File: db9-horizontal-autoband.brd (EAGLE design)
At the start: 33 x 37 mm, 19 parts, among them U8 PCA9536

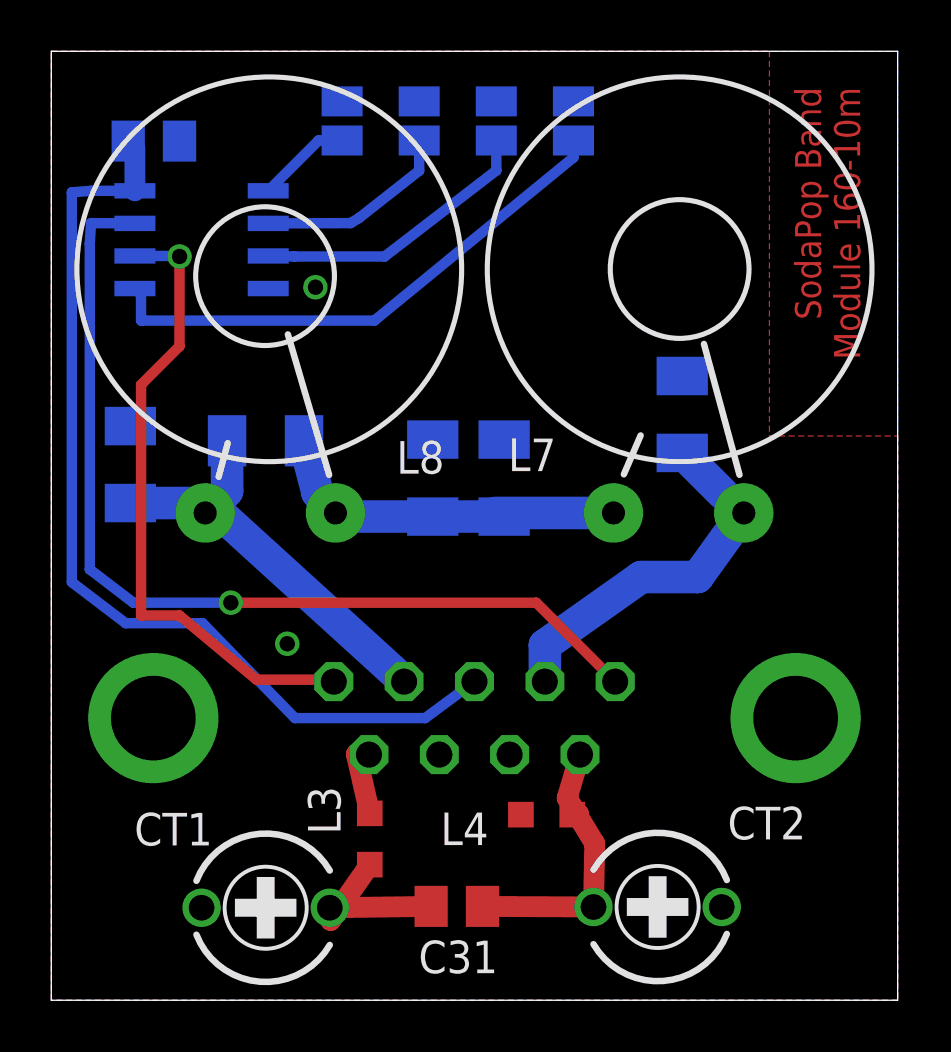
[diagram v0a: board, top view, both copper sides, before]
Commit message: Fixed hole size on trimmer cap
Fixed hole size on trimmer cap in library PCA9536.lbr and updated the
two autoband boards to use the corrected package. Package can be
replaced on other boards with the one in this library to fix the
problem. Also moved the text on the horizontal board to the bPlace
layer. Couldn't do this on the smaller board as no where to put it!
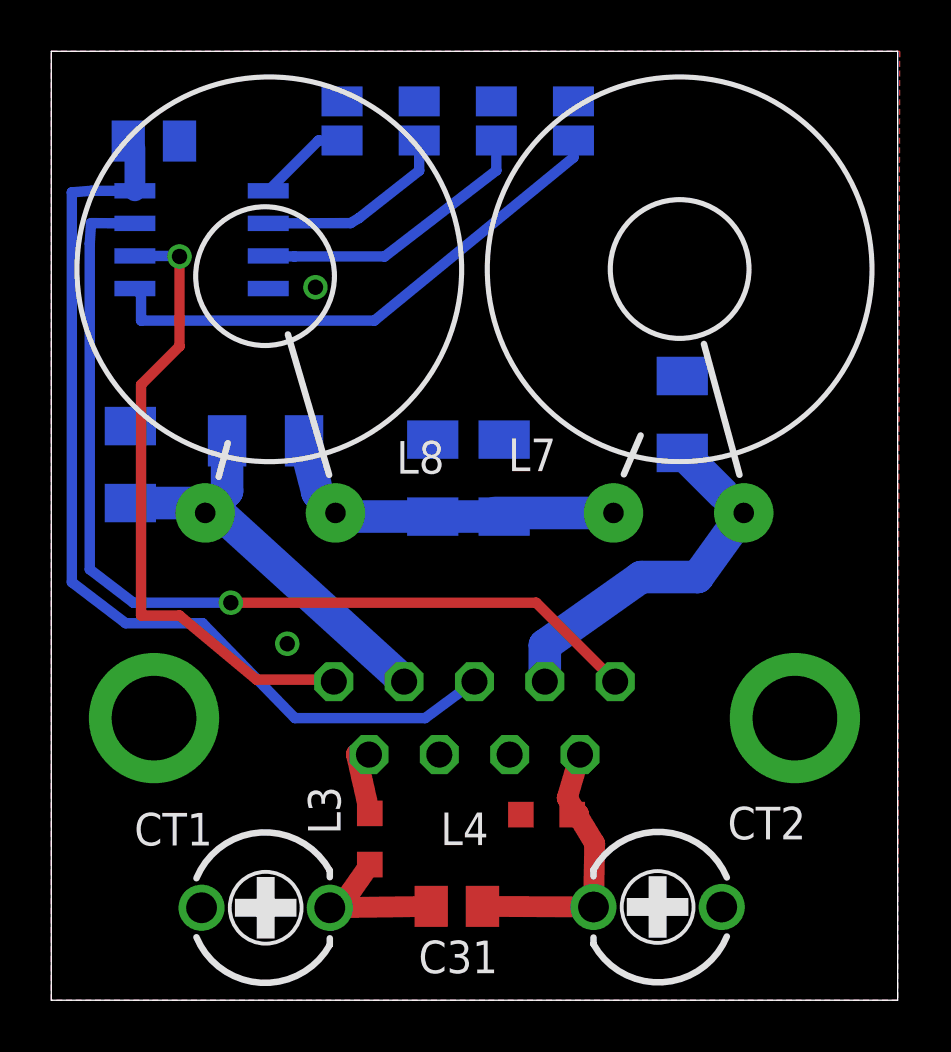
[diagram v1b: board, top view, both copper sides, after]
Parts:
- CT1, CT2: device rcl:CTRIMTZ03 -> PCA9536:CTRIMTZ03
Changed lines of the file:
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@@
 <setting verticaltext="up"/>
 </settings>
-<grid distance="0.5" unitdist="mm" unit="mm" style="lines" multiple="1" display="no" altdistance="0.1" altunitdist="mm" altunit="mm"/>
+<grid distance="1" unitdist="mm" unit="mm" style="lines" multiple="1" display="no" altdistance="0.1" altunitdist="mm" altunit="mm"/>
 <layers>
 <layer number="1" name="Top" color="4" fill="1" visible="yes" active="yes"/>
-<layer number="2" name="Route2" color="1" fill="3" visible="no" active="yes"/>
-<layer number="3" name="Route3" color="4" fill="3" visible="no" active="yes"/>
-<layer number="14" name="Route14" color="1" fill="6" visible="no" active="yes"/>
-<layer number="15" name="Route15" color="4" fill="6" visible="no" active="yes"/>
-<layer number="16" name="Bottom" color="1" fill="1" visible="no" active="yes"/>
+<layer number="2" name="Route2" color="1" fill="3" visible="yes" active="yes"/>
+<layer number="3" name="Route3" color="4" fill="3" visible="yes" active="yes"/>
+<layer number="14" name="Route14" color="1" fill="6" visible="yes" active="yes"/>
+<layer number="15" name="Route15" color="4" fill="6" visible="yes" active="yes"/>
+<layer number="16" name="Bottom" color="1" fill="1" visible="yes" active="yes"/>
 <layer number="17" name="Pads" color="2" fill="1" visible="yes" active="yes"/>
 <layer number="18" name="Vias" color="2" fill="1" visible="yes" active="yes"/>
@@
 <layer number="20" name="Dimension" color="15" fill="1" visible="yes" active="yes"/>
 <layer number="21" name="tPlace" color="7" fill="1" visible="yes" active="yes"/>
-<layer number="22" name="bPlace" color="7" fill="1" visible="no" active="yes"/>
+<layer number="22" name="bPlace" color="7" fill="1" visible="yes" active="yes"/>
 <layer number="23" name="tOrigins" color="15" fill="1" visible="yes" active="yes"/>
-<layer number="24" name="bOrigins" color="15" fill="1" visible="no" active="yes"/>
+<layer number="24" name="bOrigins" color="15" fill="1" visible="yes" active="yes"/>
 <layer number="25" name="tNames" color="7" fill="1" visible="yes" active="yes"/>
-<layer number="26" name="bNames" color="7" fill="1" visible="no" active="yes"/>
-<layer number="27" name="tValues" color="7" fill="1" visible="no" active="yes"/>
-<layer number="28" name="bValues" color="7" fill="1" visible="no" active="yes"/>
+<layer number="26" name="bNames" color="7" fill="1" visible="yes" active="yes"/>
+<layer number="27" name="tValues" color="7" fill="1" visible="yes" active="yes"/>
+<layer number="28" name="bValues" color="7" fill="1" visible="yes" active="yes"/>
 <layer number="29" name="tStop" color="7" fill="3" visible="yes" active="yes"/>
-<layer number="30" name="bStop" color="7" fill="6" visible="no" active="yes"/>
-<layer number="31" name="tCream" color="7" fill="4" visible="no" active="yes"/>
-<layer number="32" name="bCream" color="7" fill="5" visible="no" active="yes"/>
-<layer number="33" name="tFinish" color="6" fill="3" visible="no" active="yes"/>
-<layer number="34" name="bFinish" color="6" fill="6" visible="no" active="yes"/>
-<layer number="35" name="tGlue" color="7" fill="4" visible="no" active="yes"/>
-<layer number="36" name="bGlue" color="7" fill="5" visible="no" active="yes"/>
-<layer number="37" name="tTest" color="7" fill="1" visible="no" active="yes"/>
-<layer number="38" name="bTest" color="7" fill="1" visible="no" active="yes"/>
+<layer number="30" name="bStop" color="7" fill="6" visible="yes" active="yes"/>
+<layer number="31" name="tCream" color="7" fill="4" visible="yes" active="yes"/>
+<layer number="32" name="bCream" color="7" fill="5" visible="yes" active="yes"/>
+<layer number="33" name="tFinish" color="6" fill="3" visible="yes" active="yes"/>
+<layer number="34" name="bFinish" color="6" fill="6" visible="yes" active="yes"/>
+<layer number="35" name="tGlue" color="7" fill="4" visible="yes" active="yes"/>
+<layer number="36" name="bGlue" color="7" fill="5" visible="yes" active="yes"/>
+<layer number="37" name="tTest" color="7" fill="1" visible="yes" active="yes"/>
+<layer number="38" name="bTest" color="7" fill="1" visible="yes" active="yes"/>
 <layer number="39" name="tKeepout" color="4" fill="11" visible="yes" active="yes"/>
-<layer number="40" name="bKeepout" color="1" fill="11" visible="no" active="yes"/>
+<layer number="40" name="bKeepout" color="1" fill="11" visible="yes" active="yes"/>
 <layer number="41" name="tRestrict" color="4" fill="10" visible="yes" active="yes"/>
-<layer number="42" name="bRestrict" color="1" fill="10" visible="no" active="yes"/>
-<layer number="43" name="vRestrict" color="2" fill="10" visible="no" active="yes"/>
-<layer number="44" name="Drills" color="7" fill="1" visible="no" active="yes"/>
-<layer number="45" name="Holes" color="7" fill="1" visible="no" active="yes"/>
-<layer number="46" name="Milling" color="3" fill="1" visible="no" active="yes"/>
-<layer number="47" name="Measures" color="7" fill="1" visible="no" active="yes"/>
-<layer number="48" name="Document" color="7" fill="1" visible="no" active="yes"/>
-<layer number="49" name="Reference" color="7" fill="1" visible="no" active="yes"/>
-<layer number="51" name="tDocu" color="7" fill="1" visible="no" active="yes"/>
-<layer number="52" name="bDocu" color="7" fill="1" visible="no" active="yes"/>
+<layer number="42" name="bRestrict" color="1" fill="10" visible="yes" active="yes"/>
+<layer number="43" name="vRestrict" color="2" fill="10" visible="yes" active="yes"/>
+<layer number="44" name="Drills" color="7" fill="1" visible="yes" active="yes"/>
+<layer number="45" name="Holes" color="7" fill="1" visible="yes" active="yes"/>
+<layer number="46" name="Milling" color="3" fill="1" visible="yes" active="yes"/>
+<layer number="47" name="Measures" color="7" fill="1" visible="yes" active="yes"/>
+<layer number="48" name="Document" color="7" fill="1" visible="yes" active="yes"/>
+<layer number="49" name="Reference" color="7" fill="1" visible="yes" active="yes"/>
+<layer number="51" name="tDocu" color="7" fill="1" visible="yes" active="yes"/>
+<layer number="52" name="bDocu" color="7" fill="1" visible="yes" active="yes"/>
 <layer number="90" name="Modules" color="5" fill="1" visible="no" active="no"/>
 <layer number="91" name="Nets" color="2" fill="1" visible="no" active="no"/>
@@
 <wire x1="25.448" y1="25.588" x2="26.833" y2="20.487" width="0.254" layer="21"/>
 <wire x1="6.525" y1="20.405" x2="6.879" y2="21.721" width="0.254" layer="21"/>
-<text x="29" y="35.6" size="1.016" layer="1" font="vector" ratio="16" rot="R270">SodaPop Band
-Module 160-10m</text>
+<text x="3.77" y="1.06" size="1.016" layer="26" font="vector" ratio="16">SodaPop Band Module 160-10m</text>
 <wire x1="22.325" y1="20.505" x2="22.979" y2="22.021" width="0.254" layer="21"/>
 <rectangle x1="26.1" y1="21.1" x2="32.6" y2="36.6" layer="22"/>
+<wire x1="0" y1="0" x2="0" y2="37" width="1.016" layer="41"/>
+<wire x1="0" y1="37" x2="33" y2="37" width="1.016" layer="41"/>
+<wire x1="33" y1="37" x2="33" y2="0" width="1.016" layer="41"/>
+<wire x1="33" y1="0" x2="0" y2="0" width="1.016" layer="41"/>
+<wire x1="0" y1="0" x2="0" y2="37" width="1.016" layer="42"/>
+<wire x1="0" y1="37" x2="33" y2="37" width="1.016" layer="42"/>
+<wire x1="33" y1="37" x2="33" y2="0" width="1.016" layer="42"/>
+<wire x1="33" y1="0" x2="0" y2="0" width="1.016" layer="42"/>
 </plain>
 <attributes>
@@
 </autorouter>
 <elements>
-<element name="CT1" library="rcl" package="CTRIMTZ03" value="60p" x="8.359" y="3.606" smashed="yes" rot="R90">
+<element name="CT1" library="PCA9536" package="CTRIMTZ03" value="60p" x="8.359" y="3.606" smashed="yes" rot="R90">
 <attribute name="NAME" x="6.286" y="7.305" size="1.27" layer="25" rot="R180"/>
 </element>
-<element name="CT2" library="rcl" package="CTRIMTZ03" value="60p" x="23.641" y="3.636" smashed="yes" rot="R270">
+<element name="CT2" library="PCA9536" package="CTRIMTZ03" value="60p" x="23.641" y="3.636" smashed="yes" rot="R270">
 <attribute name="NAME" x="26.372" y="6.272" size="1.27" layer="25"/>
 </element>
@@
 <vertex x="0" y="0"/>
 <vertex x="0" y="37"/>
-<vertex x="28" y="37"/>
-<vertex x="28" y="22"/>
-<vertex x="33" y="22"/>
+<vertex x="33.08" y="37"/>
 <vertex x="33" y="0"/>
 </polygon>
@@
 </board>
 </drawing>
-<compatibility>
-<note version="6.3" minversion="6.2.2" severity="warning">
-Since Version 6.2.2 text objects can contain more than one line,
-which will not be processed correctly with this version.
-</note>
-</compatibility>
 </eagle>
